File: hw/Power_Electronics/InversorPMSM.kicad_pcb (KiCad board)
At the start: 4 copper layers, 150 x 90 mm, 156 parts, among them J1 FROM_CONTROL_BOARD, J2 POWER_INPUT, J3 OUTPUT POWER, Q1 HY1908D, Q2 HY1908D, Q3 HY1908D, Q4 HY1908D, Q5 HY1908D, Q6 HY1908D, U1 STDRIVE601, U2 AMS1117, U3 TSV912IDT, U4 TSV912IDT

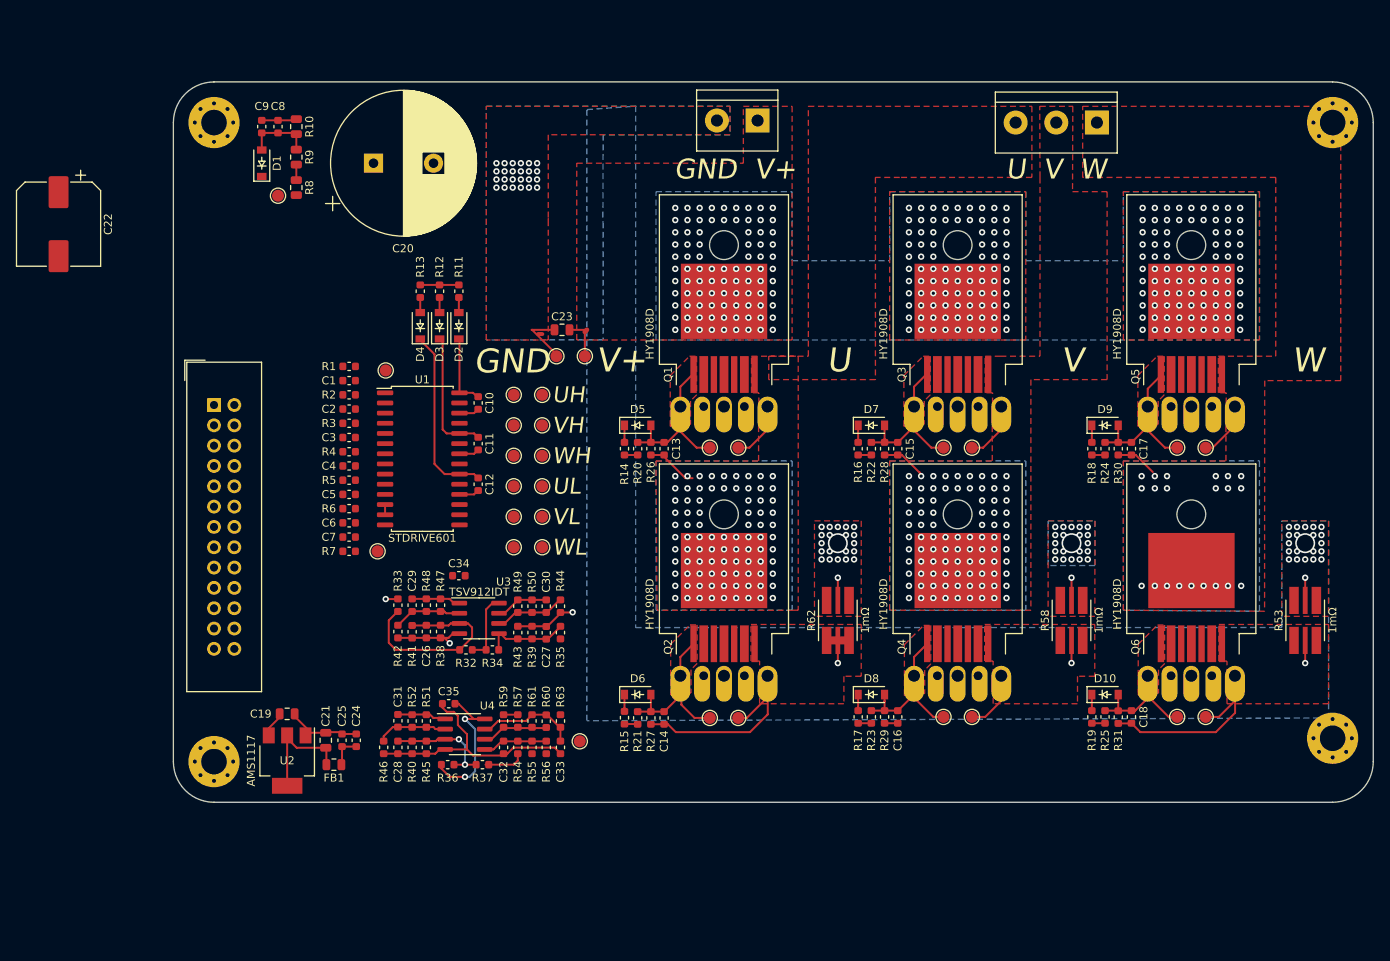
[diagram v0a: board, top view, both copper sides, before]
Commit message: all component's positions are more or less defined
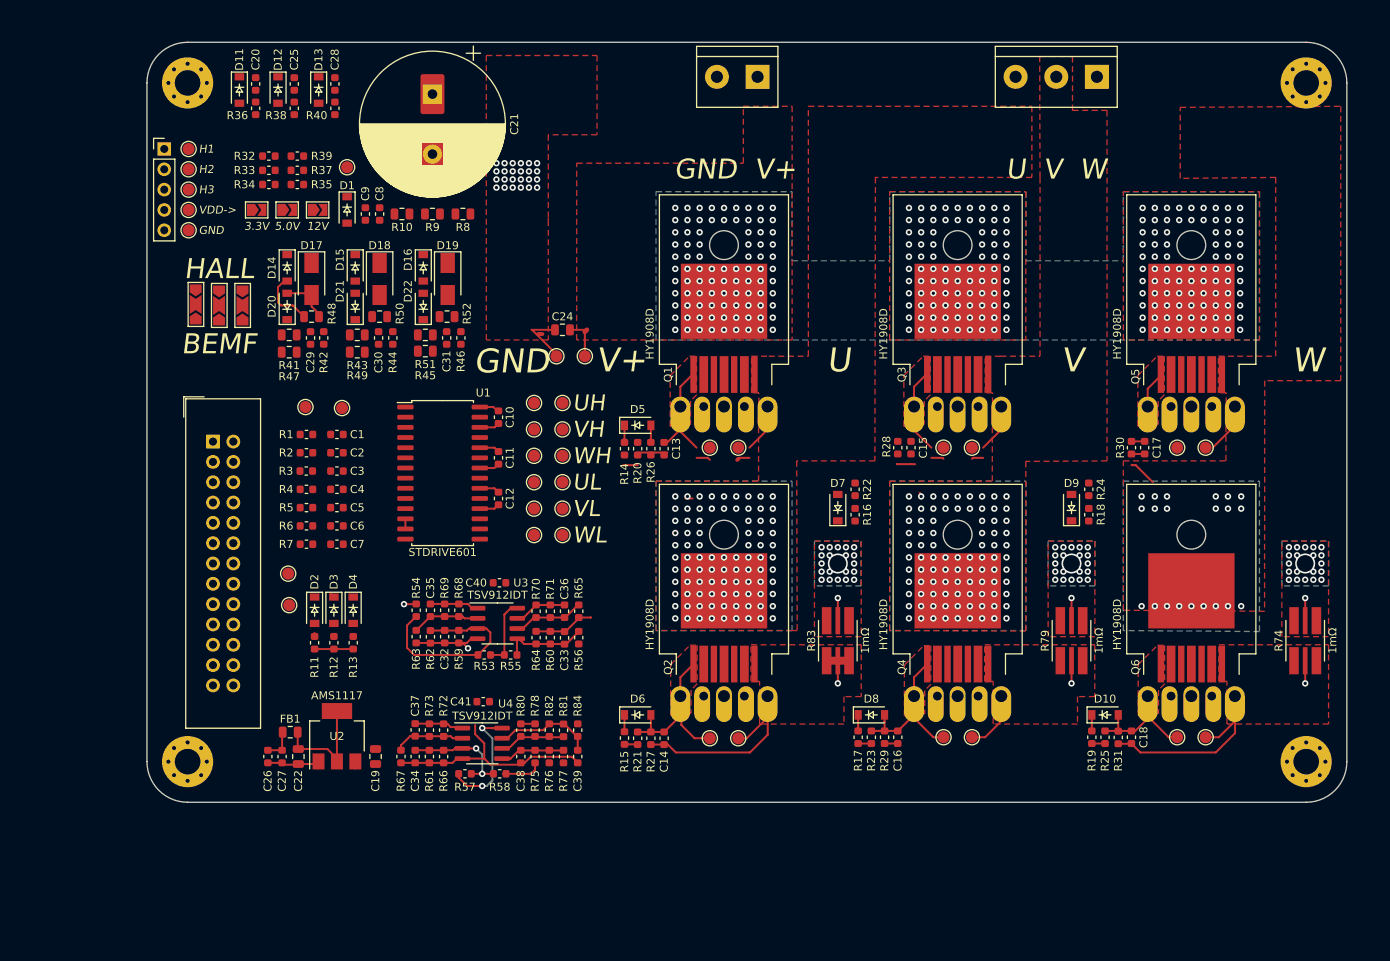
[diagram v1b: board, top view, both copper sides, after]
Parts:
- removed the C22 at (72.6, 83.8)
- added C20: 10pF, Capacitor_SMD:C_0603_1608Metric, F.Cu at (97.3, 66.3)
- added C25: 10pF, Capacitor_SMD:C_0603_1608Metric, F.Cu at (102.1, 66.3)
- added C28: 10pF, Capacitor_SMD:C_0603_1608Metric, F.Cu at (107.2, 66.3)
- added C29: 10pF, Capacitor_SMD:C_0603_1608Metric, F.Cu at (104.1, 98.0)
- added C30: 10pF, Capacitor_SMD:C_0603_1608Metric, F.Cu at (112.6, 98.0)
- added C31: 10pF, Capacitor_SMD:C_0603_1608Metric, F.Cu at (121.2, 98.0)
- added D11: B5819W, inversor-pmsm:D_SOD-123, F.Cu at (95.2, 67.1)
- added D12: B5819W, inversor-pmsm:D_SOD-123, F.Cu at (100.1, 67.1)
- added D13: B5819W, inversor-pmsm:D_SOD-123, F.Cu at (105.2, 67.1)
- added D14: B5819W, inversor-pmsm:D_SOD-123, F.Cu at (101.2, 89.3)
- added D15: B5819W, inversor-pmsm:D_SOD-123, F.Cu at (109.7, 89.3)
- added D16: B5819W, inversor-pmsm:D_SOD-123, F.Cu at (118.2, 89.3)
- added D17: RS1J, Diode_SMD:D_SMA, F.Cu at (104.3, 90.7)
- added D18: RS1J, Diode_SMD:D_SMA, F.Cu at (112.8, 90.7)
- added D19: RS1J, Diode_SMD:D_SMA, F.Cu at (121.3, 90.7)
- added D20: B5819W, inversor-pmsm:D_SOD-123, F.Cu at (101.2, 94.1)
- added D21: B5819W, inversor-pmsm:D_SOD-123, F.Cu at (109.7, 94.1)
- added D22: B5819W, inversor-pmsm:D_SOD-123, F.Cu at (118.2, 94.1)
- added J2: HALL_CONNECTOR, Connector_PinHeader_2.54mm:PinHeader_1x05_P2.54mm_Vertical, F.Cu at (85.9, 74.4)
- added JP1: Jumper_2_Open, Jumper:SolderJumper-2_P1.3mm_Open_TrianglePad1.0x1.5mm, F.Cu at (97.4, 82.0)
- added JP2: Jumper_2_Open, Jumper:SolderJumper-2_P1.3mm_Open_TrianglePad1.0x1.5mm, F.Cu at (101.2, 82.0)
- added JP3: Jumper_2_Open, Jumper:SolderJumper-2_P1.3mm_Open_TrianglePad1.0x1.5mm, F.Cu at (105.0, 82.0)
- added JP4: Jumper_3_Open, inversor-pmsm:SolderJumper-3_P2.0mm_Open_TrianglePad1.0x1.5mm_custom, F.Cu at (95.6, 94.0)
- added JP5: Jumper_3_Open, inversor-pmsm:SolderJumper-3_P2.0mm_Open_TrianglePad1.0x1.5mm_custom, F.Cu at (92.7, 94.0)
- added JP6: Jumper_3_Open, inversor-pmsm:SolderJumper-3_P2.0mm_Open_TrianglePad1.0x1.5mm_custom, F.Cu at (89.8, 93.9)
- added R32: 2K, Resistor_SMD:R_0603_1608Metric, F.Cu at (98.9, 75.3)
- added R33: 2K, Resistor_SMD:R_0603_1608Metric, F.Cu at (98.9, 77.1)
- added R34: 2K, Resistor_SMD:R_0603_1608Metric, F.Cu at (98.9, 78.9)
- added R35: 10K, Resistor_SMD:R_0603_1608Metric, F.Cu at (102.5, 78.9)
- added R36: DNM, Resistor_SMD:R_0603_1608Metric, F.Cu at (97.3, 69.3)
- added R37: 10K, Resistor_SMD:R_0603_1608Metric, F.Cu at (102.5, 77.1)
- added R38: DNM, Resistor_SMD:R_0603_1608Metric, F.Cu at (102.1, 69.3)
- added R39: 10K, Resistor_SMD:R_0603_1608Metric, F.Cu at (102.5, 75.3)
- added R40: DNM, Resistor_SMD:R_0603_1608Metric, F.Cu at (107.2, 69.3)
- added R41: 100K, Resistor_SMD:R_0805_2012Metric, F.Cu at (101.5, 99.8)
- added R42: 1K, Resistor_SMD:R_0603_1608Metric, F.Cu at (105.8, 98.0)
- added R43: 100K, Resistor_SMD:R_0805_2012Metric, F.Cu at (110.0, 99.8)
- added R44: 1K, Resistor_SMD:R_0603_1608Metric, F.Cu at (114.4, 98.0)
- added R45: 100K, Resistor_SMD:R_0805_2012Metric, F.Cu at (118.5, 97.7)
- added R46: 1K, Resistor_SMD:R_0603_1608Metric, F.Cu at (122.9, 98.0)
- added R47: 100K, Resistor_SMD:R_0805_2012Metric, F.Cu at (101.5, 97.7)
- added R48: 5.6K, Resistor_SMD:R_0805_2012Metric, F.Cu at (104.3, 95.4)
- added R49: 100K, Resistor_SMD:R_0805_2012Metric, F.Cu at (110.0, 97.7)
- added R50: 5.6K, Resistor_SMD:R_0805_2012Metric, F.Cu at (112.8, 95.4)
- added R51: 100K, Resistor_SMD:R_0805_2012Metric, F.Cu at (118.5, 99.7)
- added R52: 5.6K, Resistor_SMD:R_0805_2012Metric, F.Cu at (121.2, 95.4)
- added TP31: TestPoint, TestPoint:TestPoint_Pad_D1.5mm, F.Cu at (108.1, 106.8)
- added TP32: TestPoint, TestPoint:TestPoint_Pad_D1.5mm, F.Cu at (88.9, 84.6)
- added TP33: TestPoint, TestPoint:TestPoint_Pad_D1.5mm, F.Cu at (88.9, 82.0)
- added TP34: TestPoint, TestPoint:TestPoint_Pad_D1.5mm, F.Cu at (88.9, 79.5)
- added TP35: TestPoint, TestPoint:TestPoint_Pad_D1.5mm, F.Cu at (88.9, 77.0)
- added TP36: TestPoint, TestPoint:TestPoint_Pad_D1.5mm, F.Cu at (88.9, 74.4)
- C21: renamed from C20; footprint Capacitor_THT:CP_Radial_D18.0mm_P7.50mm -> inversor-pmsm:CP_Radial_D18.0mm_P7.50mm_universal
- moved R11 47.5 mm to (104.6, 136.1), turned to 270 degrees
- moved R12 45.9 mm to (107.1, 136.1), turned to 270 degrees
- moved R13 44.7 mm to (109.5, 136.1), turned to 270 degrees
- moved TP30 40.1 mm to (101.5, 131.4)
- moved D2 39.9 mm to (104.6, 132.1), turned to 270 degrees
- moved D3 37.9 mm to (107.1, 132.1), turned to 270 degrees
- moved D4 36.5 mm to (109.5, 132.1), turned to 270 degrees
- moved R8 21.1 mm to (123.2, 82.5), turned to 180 degrees
- moved R9 18.4 mm to (119.4, 82.5), turned to 0 degrees
- moved R10 17.1 mm to (115.6, 82.5), turned to 180 degrees
- moved C9 16.9 mm to (111.0, 82.5)
- moved C8 16.8 mm to (112.8, 82.5)
- moved C19 12.3 mm to (112.3, 150.4), turned to 270 degrees
- moved D1 12.2 mm to (108.7, 82.0), turned to 270 degrees
- moved TP1 11.5 mm to (101.3, 127.5)
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- renumbered C21 to C22, C23 to C24, C24 to C26, C25 to C27, C26 to C32, C27 to C33, C28 to C34, C29 to C35, C30 to C36, C31 to C37, C32 to C38, C33 to C39, C34 to C40, C35 to C41, J2 to J3, J3 to J4, R32 to R53, R33 to R54, R34 to R55, R35 to R56, R36 to R57, R37 to R58, R38 to R59, R39 to R60, R40 to R61, R41 to R62, R42 to R63, R43 to R64, R44 to R65, R45 to R66, R46 to R67, R47 to R68, R48 to R69, R49 to R70, R50 to R71, R51 to R72, R52 to R73, R53 to R74, R54 to R75, R55 to R76, R56 to R77, R57 to R78, R58 to R79, R59 to R80, R60 to R81, R61 to R82, R62 to R83, R63 to R84, TP7 to TP10, TP8 to TP11, TP9 to TP12, TP10 to TP13, TP11 to TP14, TP12 to TP15, TP13 to TP16, TP14 to TP17, TP15 to TP18, TP16 to TP19, TP17 to TP20, TP18 to TP21, TP19 to TP22, TP20 to TP23, TP21 to TP24, TP22 to TP25, TP23 to TP26, TP24 to TP27, TP25 to TP28, TP26 to TP29, TP27 to TP30, TP28 to TP4, TP29 to TP5, TP30 to TP6, TP4 to TP7, TP5 to TP8, TP6 to TP9
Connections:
- H1 pad 1: Net-(H1-Pad1) -> SENSE1_REF
- H2 pad 1: Net-(H2-Pad1) -> SENSE1_REF
- H3 pad 1: Net-(H3-Pad1) -> SENSE1_REF
- H4 pad 1: Net-(H4-Pad1) -> SENSE1_REF
- J3 pad 1: HV -> SENSE1_REF
- J3 pad 2: SENSE1_REF -> HV
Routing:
- net SENSE1_REF: track 139.2 -> 82.0 mm, vias 92 -> 91
- net SENSE1: track 91.4 -> 42.9 mm
- net /BOOT3: track 22.7 -> 2.93 mm
- net /BOOT2: track 16.5 -> 3.34 mm
- net /GH3: track 19.1 -> 7.69 mm
- net /GH2: track 19.6 -> 10.7 mm
- net VBUS_SCALED: track 8.61 -> 0.00 mm
- net Net-(D14-Pad2): track 0.00 -> 7.35 mm
- net BEMF_A: track 0.00 -> 6.91 mm
- net /BOOT1: track 10.6 -> 3.81 mm
- net OUT1: track 17.9 -> 12.1 mm
- net +3V3: track 32.4 -> 29.3 mm
- net OUT2: track 13.6 -> 10.5 mm
- net +5V: track 3.35 -> 1.02 mm
- net Net-(D9-Pad1): track 2.13 -> 0.00 mm
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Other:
- board size 150 x 90 mm -> 150 x 95 mm
- board text added: "12V"
- board text added: "3.3V"
- board text added: "5.0V"
- board text added: "BEMF"
- board text added: "H1"
- board text added: "H2"
- board text added: "H3"
- board text added: "HALL"
- board text added: "VDD->"

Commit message: further advances made on the layout
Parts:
- removed J3: POWER_INPUT, TerminalBlock:TerminalBlock_bornier-2_P5.08mm
- removed J4: OUTPUT POWER, TerminalBlock:TerminalBlock_bornier-3_P5.08mm
- added C42: DNM, Capacitor_SMD:C_0603_1608Metric, F.Cu at (100.3, 168.3)
- added C43: DNM, Capacitor_SMD:C_0603_1608Metric, F.Cu at (100.3, 170.8)
- added C44: DNM, Capacitor_SMD:C_0603_1608Metric, F.Cu at (108.0, 142.7)
- added C45: 33pF, Capacitor_SMD:C_0603_1608Metric, F.Cu at (100.3, 173.3)
- added H5: MountingHole_Pad, inversor-pmsm:MountingHole_3.4mm_M3_Pad_Via, F.Cu at (160.4, 65.5)
- added H6: MountingHole_Pad, inversor-pmsm:MountingHole_3.4mm_M3_Pad_Via, F.Cu at (188.7, 65.5)
- added H7: MountingHole_Pad, inversor-pmsm:MountingHole_3.4mm_M3_Pad_Via, F.Cu at (149.7, 65.5)
- added H8: MountingHole_Pad, inversor-pmsm:MountingHole_3.4mm_M3_Pad_Via, F.Cu at (199.4, 65.5)
- added H9: MountingHole_Pad, inversor-pmsm:MountingHole_3.4mm_M3_Pad_Via, F.Cu at (209.9, 65.5)
- added J5: MEASURE_CONN, Connector_PinHeader_2.54mm:PinHeader_1x13_P2.54mm_Vertical, F.Cu at (85.9, 111.0)
- added JP7: Jumper, Jumper:SolderJumper-2_P1.3mm_Open_TrianglePad1.0x1.5mm, F.Cu at (86.4, 93.9)
- added R85: 10K, Resistor_SMD:R_0603_1608Metric, F.Cu at (198.4, 106.2)
- added R86: 10K, Resistor_SMD:R_0603_1608Metric, F.Cu at (200.7, 106.2)
- added R87: 1K, Resistor_SMD:R_0603_1608Metric, F.Cu at (104.3, 170.8)
- added R88: 1K, Resistor_SMD:R_0603_1608Metric, F.Cu at (111.3, 141.0)
- added R89: 1K, Resistor_SMD:R_0603_1608Metric, F.Cu at (111.3, 142.7)
- added R90: 100K, Resistor_SMD:R_0603_1608Metric, F.Cu at (108.3, 170.8)
- added R91: 100K, Resistor_SMD:R_0603_1608Metric, F.Cu at (112.4, 168.3)
- added R92: 1K, Resistor_SMD:R_0603_1608Metric, F.Cu at (108.3, 173.3)
- moved D5 20.8 mm to (142.7, 129.7), turned to 90 degrees
- moved R14 18.7 mm to (144.9, 130.6), turned to 90 degrees
- moved C19 18.3 mm to (94.0, 150.1)
- moved R20 15.5 mm to (144.9, 127.4)
- moved TP30 11.9 mm to (112.3, 126.5)
- moved TP1 6.90 mm to (108.2, 126.7)
- moved C1 6.14 mm to (113.5, 109.3)
- moved C2 6.14 mm to (113.5, 111.6)
- moved C3 6.14 mm to (113.5, 113.9)
- moved C4 6.14 mm to (113.5, 116.2)
- moved C5 6.14 mm to (113.5, 118.5)
- moved C6 6.14 mm to (113.5, 120.8)
- moved C7 6.14 mm to (113.5, 123.1)
- moved R3 6.14 mm to (109.7, 113.9)
- moved TP2 6.14 mm to (109.6, 105.9)
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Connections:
- net Net-(J1-Pad10) renamed /PWM_W_H
- net Net-(J1-Pad12) renamed /PWM_U_L
- net Net-(J1-Pad14) renamed /PWM_V_L
- net Net-(J1-Pad16) renamed /PWM_W_L
- net Net-(J1-Pad6) renamed /PWM_U_H
- net Net-(J1-Pad8) renamed /PWM_V_H
- net ~ERROR renamed ~FAULT
- J1 pad 11: SENSE_OUT2 -> SENSE2
- J1 pad 13: SENSE_OUT3 -> SENSE3
- J1 pad 7: Net-(J1-Pad7) -> NTC_TEMP
- J1 pad 9: SENSE_OUT1 -> SENSE1
- U1 pad 10: ENABLE -> /EN
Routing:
- net /GL1: track 19.4 -> 5.07 mm
- net SENSE1: track 42.9 -> 32.3 mm
- net /GH1: track 24.1 -> 14.4 mm
- net Net-(C22-Pad1): track 14.3 -> 8.76 mm
- net SENSE1_REF: track 82.0 -> 78.0 mm
- net OUT2: track 10.5 -> 6.77 mm
- net OUT3: track 12.1 -> 8.47 mm
- net +3V3: track 29.3 -> 27.0 mm
- net Net-(D6-Pad1): track 2.24 -> 0.00 mm
- net Net-(D5-Pad1): track 2.01 -> 0.00 mm
- net Net-(R15-Pad2): track 1.92 -> 0.00 mm
- net Net-(R14-Pad2): track 1.79 -> 0.00 mm
- net /GH2: track 10.7 -> 9.08 mm
- net OUT1: track 12.1 -> 10.8 mm
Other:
- board text added: "~FLT"
